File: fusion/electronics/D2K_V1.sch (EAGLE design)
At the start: 24 parts, among them M1 Active Cooler SC1148, SW1 BTN_DPAD_UP, SW10 BTN_SELECT, SW11 BTN_HOME, SW12 BTN_L1, SW13 BTN_R1, SW14 BTN_L2, SW15 BTN_R2, SW2 BTN_DPAD_DOWN, SW3 BTN_DPAD_LEFT, SW4 BTN_DPAD_RIGHT, SW5 BTN_A, SW6 BTN_B, SW7 BTN_X, SW8 BTN_Y, SW9 BTN_START, U1 Raspberry Pi 5, U2 ESP32-S3-Zero - USB HID, U3 WM8960 Audio Board

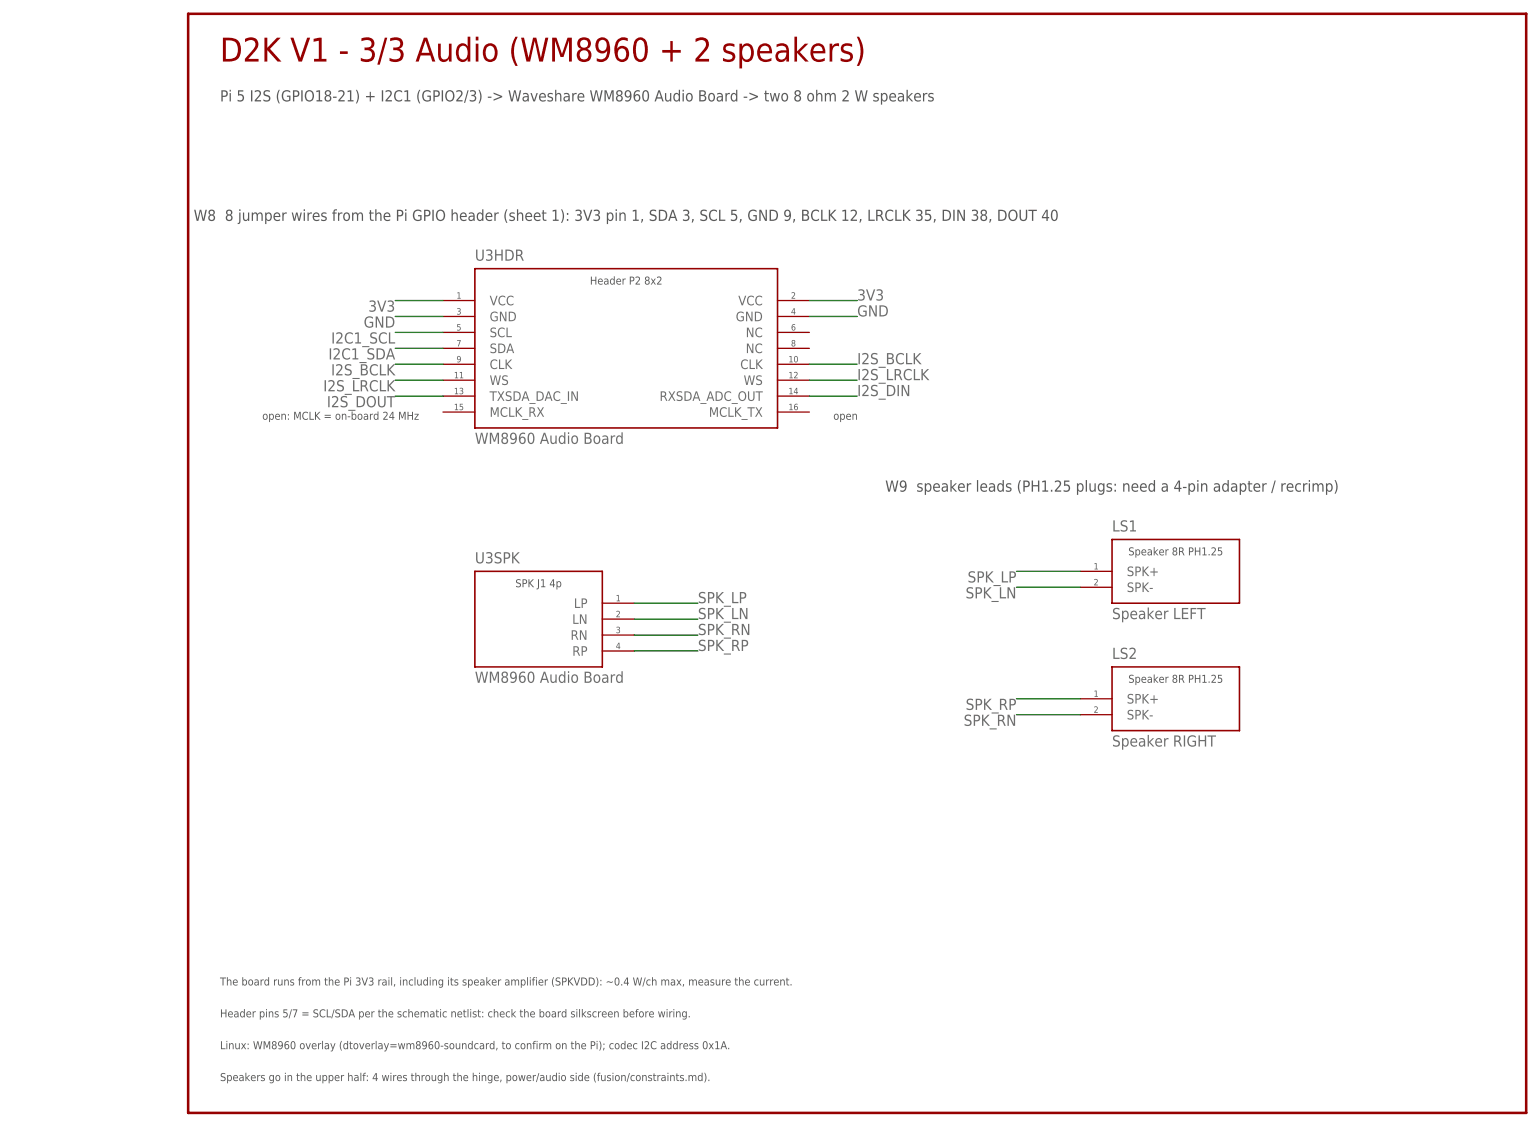
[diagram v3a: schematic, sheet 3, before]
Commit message: WM8960 audio board: verified header pinout, 24 MHz overlay
Bench-tested on the Pi 5 with a headset on the board's jack.

- Header P2: 5 = SDA, 7 = SCL (was swapped), 13 = RXSDA is the DAC
  input (Pi DOUT), 14 = TXSDA the mic output (Pi DIN), as on the
  silkscreen and Waveshare's schematic. Breadboard page, library and
  schematic regenerated; wire table names each silkscreen label.
- Second GND wire (Pi 39 to header pin 4) beside the I2S wires.
- scripts/linux/overlays/d2k-wm8960-24mhz.dts: the firmware's
  wm8960-soundcard with MCLK 24 MHz, the board's oscillator.
- docs/platform.md: overlay, mixer and the wiring faults met on the
  bench with their symptoms; Q18 answered.

Co-Authored-By: Claude Opus 5.5 <noreply@anthropic.com>
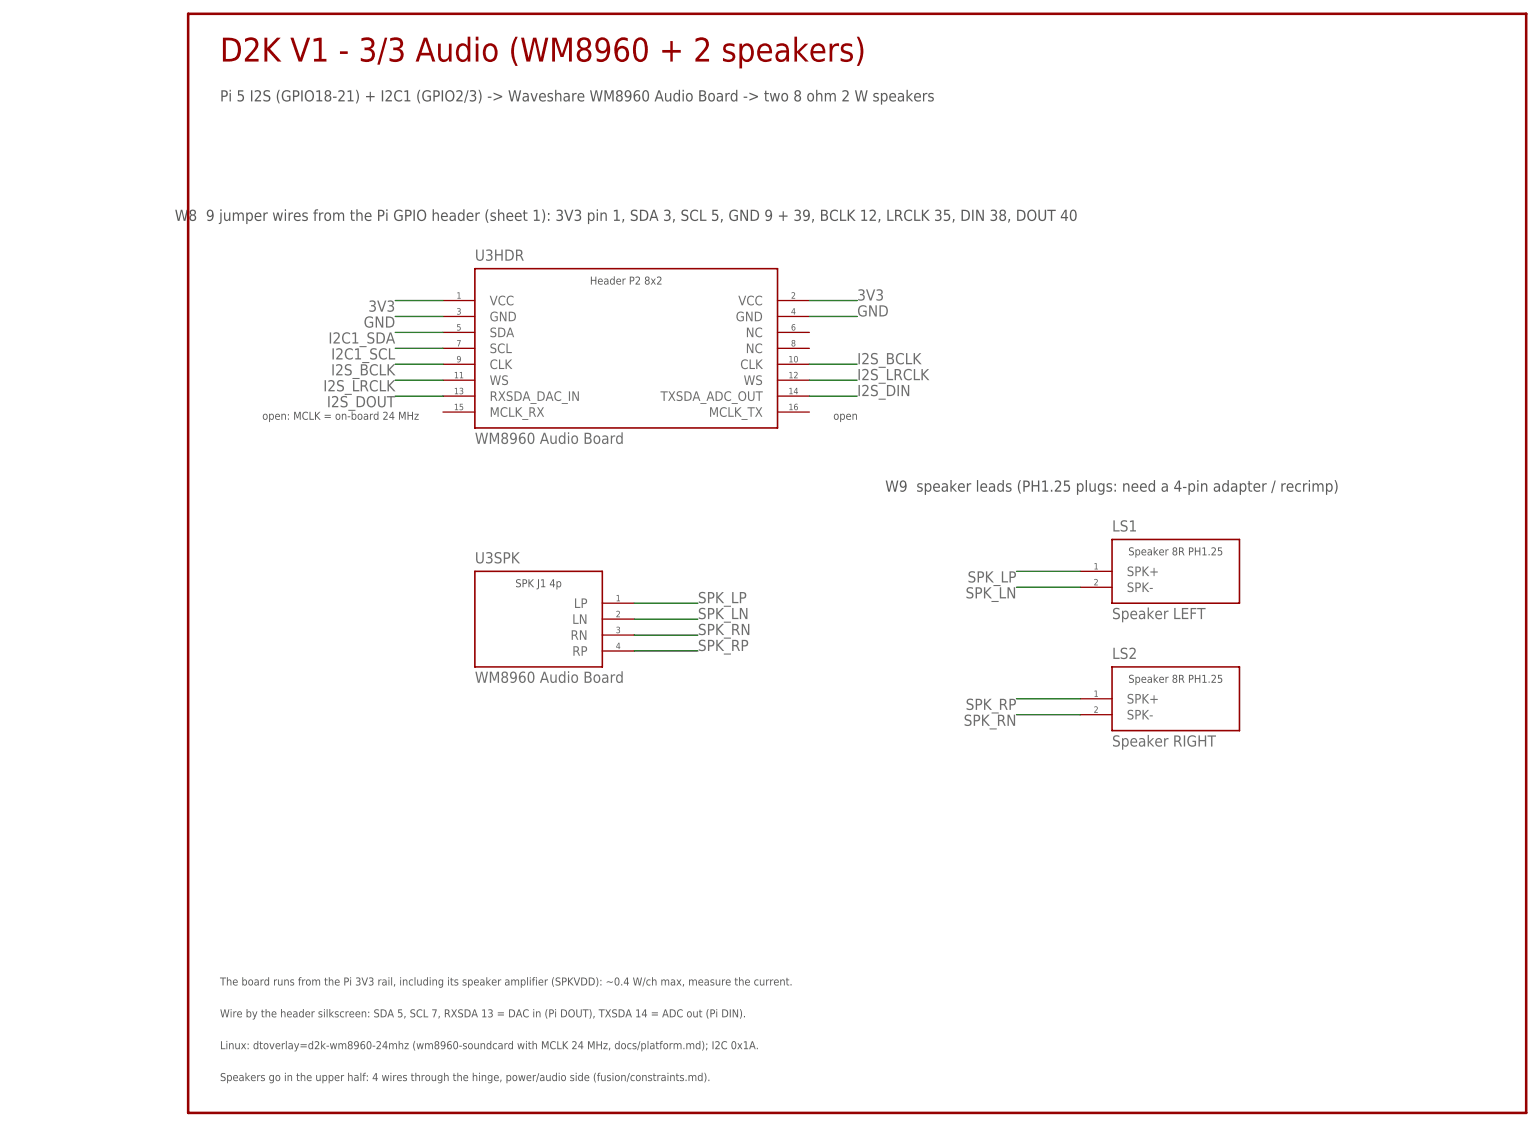
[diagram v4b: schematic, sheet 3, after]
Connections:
- net GND: now also U1GPIO.GND@8
- net I2S_DIN: now also U3HDR.TXSDA_ADC_OUT; no longer U3HDR.RXSDA_ADC_OUT
- net I2S_DOUT: now also U3HDR.RXSDA_DAC_IN; no longer U3HDR.TXSDA_DAC_IN
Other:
- note added: "Labelled pins 1, 3, 5, 9, 12, 35, 38, 39, 40: WM8960 audio board (sheet 3), W8 jumper wires."
- note added: "Linux: dtoverlay=d2k-wm8960-24mhz (wm8960-soundcard with MCLK 24 MHz, docs/platform.md); I2C 0x1A."
- note added: "W8 9 jumper wires from the Pi GPIO header (sheet 1): 3V3 pin 1, SDA 3, SCL 5, GND 9 + 39, BCLK 12, LRCLK 35, DIN 38, DOUT 40"
- note added: "Wire by the header silkscreen: SDA 5, SCL 7, RXSDA 13 = DAC in (Pi DOUT), TXSDA 14 = ADC out (Pi DIN)."
- note removed: "Header pins 5/7 = SCL/SDA per the schematic netlist: check the board silkscreen before wiring."
- note removed: "Labelled pins 1, 3, 5, 9, 12, 35, 38, 40: WM8960 audio board (sheet 3), W8 jumper wires."
- note removed: "Linux: WM8960 overlay (dtoverlay=wm8960-soundcard, to confirm on the Pi); codec I2C address 0x1A."
- note removed: "W8 8 jumper wires from the Pi GPIO header (sheet 1): 3V3 pin 1, SDA 3, SCL 5, GND 9, BCLK 12, LRCLK 35, DIN 38, DOUT 40"
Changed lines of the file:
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@@
 <text x="314.96" y="-69.85" size="1.778" layer="97" align="bottom-center">W5  2-wire lead: red = 5V (pin 4), black = GND (pin 6)</text>
 <text x="256.54" y="-128.27" size="1.778" layer="97" align="top-center">! GPIO 5V is not fused: one pin off can kill the Pi. Power off before plugging.</text>
-<text x="256.54" y="-130.8" size="1.27" layer="97" align="top-center">Labelled pins 1, 3, 5, 9, 12, 35, 38, 40: WM8960 audio board (sheet 3), W8 jumper wires.</text>
+<text x="256.54" y="-130.8" size="1.27" layer="97" align="top-center">Labelled pins 1, 3, 5, 9, 12, 35, 38, 39, 40: WM8960 audio board (sheet 3), W8 jumper wires.</text>
 <text x="279.4" y="-138.43" size="1.778" layer="97" align="bottom-center">W6  Fan lead JST-SH 4p (captive)</text>
 <wire x1="-45.72" y1="43.18" x2="411.48" y2="43.18" width="0.4064" layer="94"/>
@@
 <wire x1="223.52" y1="-86.36" x2="215.9" y2="-86.36" width="0.1524" layer="91"/>
 <label x="215.9" y="-86.36" size="1.778" layer="95" rot="R180"/>
+</segment>
+<segment>
+<pinref part="U1" gate="GPIO" pin="GND@8"/>
+<wire x1="223.52" y1="-124.46" x2="215.9" y2="-124.46" width="0.1524" layer="91"/>
+<label x="215.9" y="-124.46" size="1.778" layer="95" rot="R180"/>
 </segment>
 <segment>
@@
 <text x="-8.89" y="-20.92" size="1.27" layer="97" align="center-right">open: MCLK = on-board 24 MHz</text>
 <text x="57.15" y="-20.92" size="1.27" layer="97" align="center-left">open</text>
-<text x="24.13" y="10.16" size="1.778" layer="97" align="bottom-center">W8  8 jumper wires from the Pi GPIO header (sheet 1): 3V3 pin 1, SDA 3, SCL 5, GND 9, BCLK 12, LRCLK 35, DIN 38, DOUT 40</text>
+<text x="24.13" y="10.16" size="1.778" layer="97" align="bottom-center">W8  9 jumper wires from the Pi GPIO header (sheet 1): 3V3 pin 1, SDA 3, SCL 5, GND 9 + 39, BCLK 12, LRCLK 35, DIN 38, DOUT 40</text>
 <text x="101.6" y="-33.02" size="1.778" layer="97" align="bottom-center">W9  speaker leads (PH1.25 plugs: need a 4-pin adapter / recrimp)</text>
 <wire x1="-45.72" y1="43.18" x2="167.64" y2="43.18" width="0.4064" layer="94"/>
@@
 <text x="-40.64" y="29.21" size="1.778" layer="97">Pi 5 I2S (GPIO18-21) + I2C1 (GPIO2/3) -&gt; Waveshare WM8960 Audio Board -&gt; two 8 ohm 2 W speakers</text>
 <text x="-40.64" y="-111.76" size="1.27" layer="97">The board runs from the Pi 3V3 rail, including its speaker amplifier (SPKVDD): ~0.4 W/ch max, measure the current.</text>
-<text x="-40.64" y="-116.84" size="1.27" layer="97">Header pins 5/7 = SCL/SDA per the schematic netlist: check the board silkscreen before wiring.</text>
-<text x="-40.64" y="-121.92" size="1.27" layer="97">Linux: WM8960 overlay (dtoverlay=wm8960-soundcard, to confirm on the Pi); codec I2C address 0x1A.</text>
+<text x="-40.64" y="-116.84" size="1.27" layer="97">Wire by the header silkscreen: SDA 5, SCL 7, RXSDA 13 = DAC in (Pi DOUT), TXSDA 14 = ADC out (Pi DIN).</text>
+<text x="-40.64" y="-121.92" size="1.27" layer="97">Linux: dtoverlay=d2k-wm8960-24mhz (wm8960-soundcard with MCLK 24 MHz, docs/platform.md); I2C 0x1A.</text>
 <text x="-40.64" y="-127" size="1.27" layer="97">Speakers go in the upper half: 4 wires through the hinge, power/audio side (fusion/constraints.md).</text>
 </plain>
@@
 <segment>
 <pinref part="U3" gate="HDR" pin="SCL"/>
+<wire x1="-5.08" y1="-10.16" x2="-12.7" y2="-10.16" width="0.1524" layer="91"/>
+<label x="-12.7" y="-10.16" size="1.778" layer="95" rot="R180"/>
+</segment>
+</net>
+<net name="I2C1_SDA" class="0">
+<segment>
+<pinref part="U3" gate="HDR" pin="SDA"/>
 <wire x1="-5.08" y1="-7.62" x2="-12.7" y2="-7.62" width="0.1524" layer="91"/>
 <label x="-12.7" y="-7.62" size="1.778" layer="95" rot="R180"/>
-</segment>
-</net>
-<net name="I2C1_SDA" class="0">
-<segment>
-<pinref part="U3" gate="HDR" pin="SDA"/>
-<wire x1="-5.08" y1="-10.16" x2="-12.7" y2="-10.16" width="0.1524" layer="91"/>
-<label x="-12.7" y="-10.16" size="1.778" layer="95" rot="R180"/>
 </segment>
 </net>
@@
 <net name="I2S_DOUT" class="0">
 <segment>
-<pinref part="U3" gate="HDR" pin="TXSDA_DAC_IN"/>
+<pinref part="U3" gate="HDR" pin="RXSDA_DAC_IN"/>
 <wire x1="-5.08" y1="-17.78" x2="-12.7" y2="-17.78" width="0.1524" layer="91"/>
 <label x="-12.7" y="-17.78" size="1.778" layer="95" rot="R180"/>
@@
 <net name="I2S_DIN" class="0">
 <segment>
-<pinref part="U3" gate="HDR" pin="RXSDA_ADC_OUT"/>
+<pinref part="U3" gate="HDR" pin="TXSDA_ADC_OUT"/>
 <wire x1="53.34" y1="-17.78" x2="60.96" y2="-17.78" width="0.1524" layer="91"/>
 <label x="60.96" y="-17.78" size="1.778" layer="95"/>
